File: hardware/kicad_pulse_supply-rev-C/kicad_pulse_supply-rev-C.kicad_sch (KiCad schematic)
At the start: 4 parts

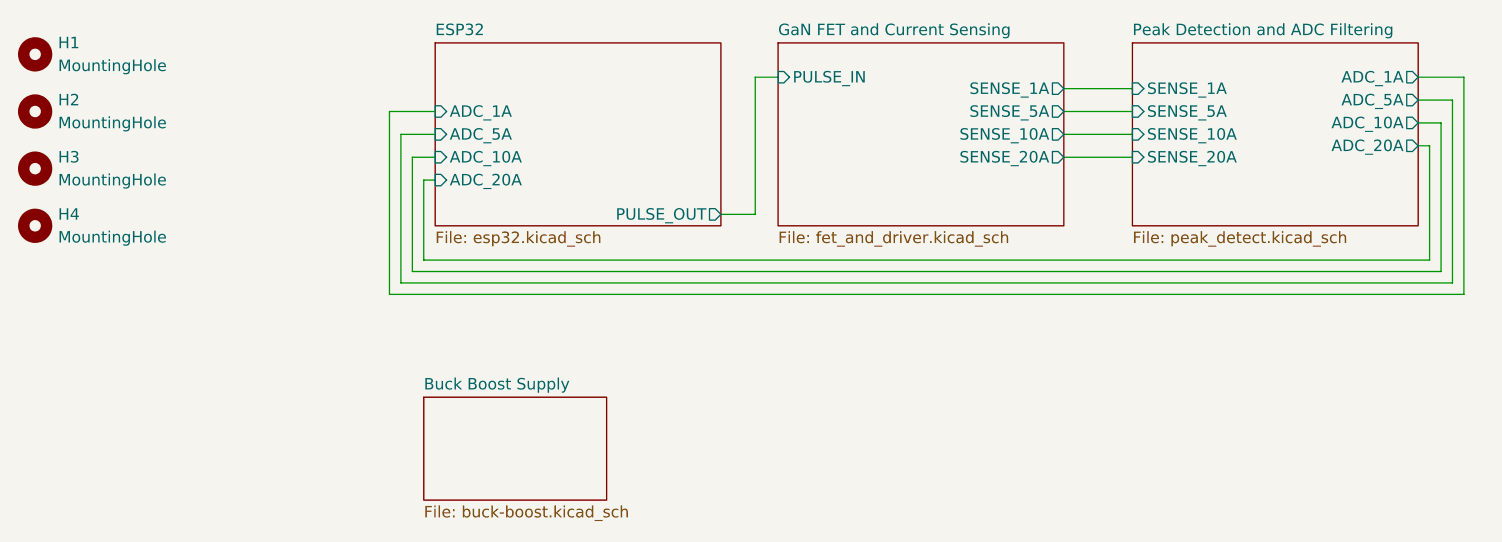
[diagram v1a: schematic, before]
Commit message: hardware breakout boards added, pcb rev-c began
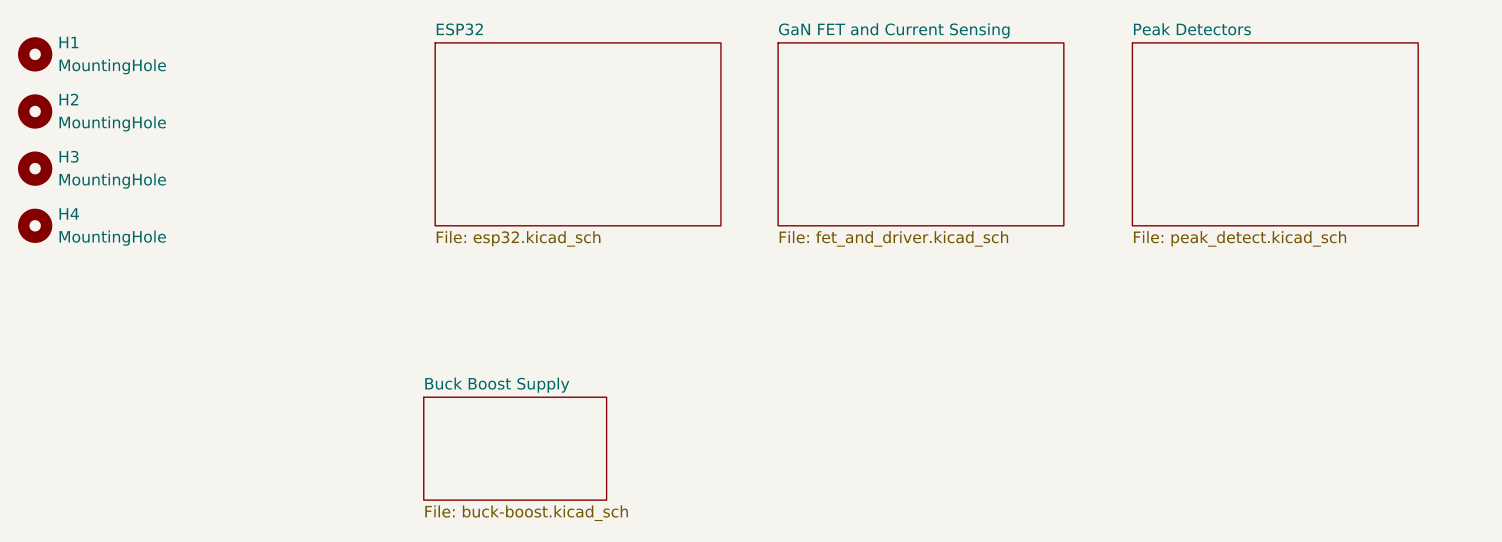
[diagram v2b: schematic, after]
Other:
- sheet Peak Detection and ADC Filtering renamed Peak Detectors
- sheet ESP32 ports: added none; removed ADC_10A, ADC_1A, ADC_20A, ADC_5A, PULSE_OUT
- sheet GaN FET and Current Sensing ports: added none; removed PULSE_IN, SENSE_10A, SENSE_1A, SENSE_20A, SENSE_5A
- sheet Peak Detectors ports: added none; removed ADC_10A, ADC_1A, ADC_20A, ADC_5A, SENSE_10A, SENSE_1A, SENSE_20A, SENSE_5A

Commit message: Rev C pcb complete, last commit before branching firmware for new board
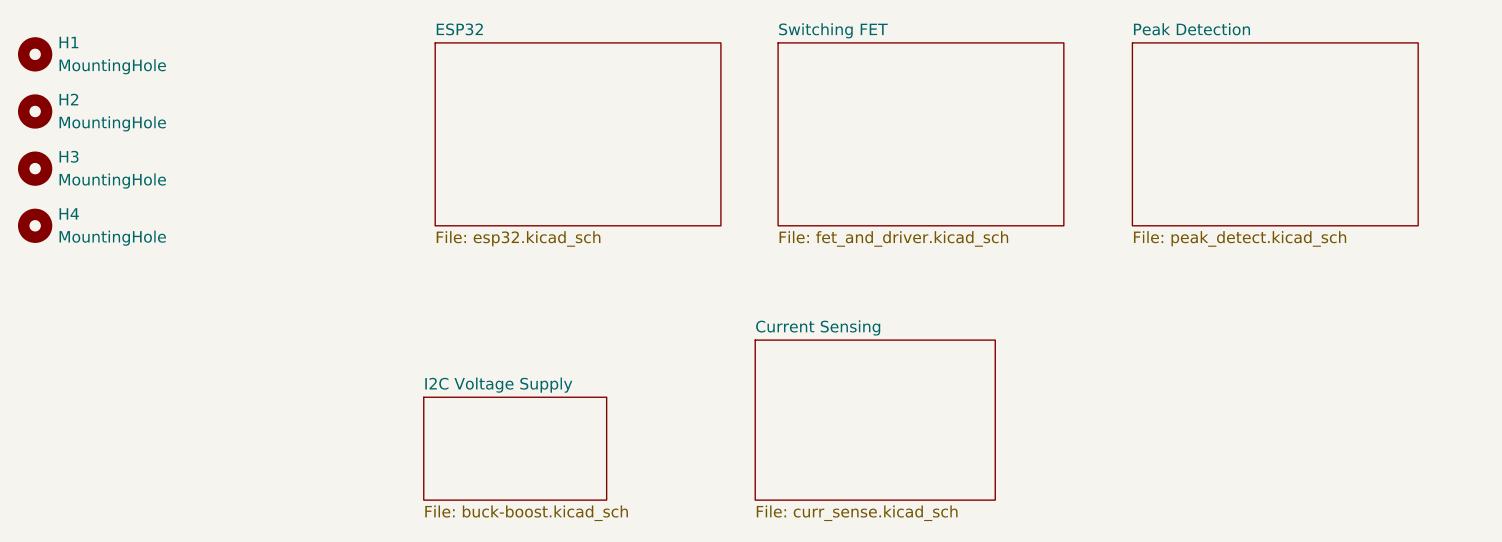
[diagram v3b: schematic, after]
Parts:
- H1, H2, H3, H4: footprint MountingHole:MountingHole_3.5mm -> MountingHole:MountingHole_3.2mm_M3
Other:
- sheet Buck Boost Supply renamed I2C Voltage Supply
- sheet GaN FET and Current Sensing renamed Switching FET
- sheet Peak Detectors renamed Peak Detection
- added sheet Current Sensing (curr_sense.kicad_sch)
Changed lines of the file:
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@@
 (kicad_sch
-	(version 20231120)
+	(version 20250114)
 	(generator "eeschema")
-	(generator_version "8.0")
+	(generator_version "9.0")
 	(paper "A4")
 	(title_block
@@
 			)
 		)
-		(property "Footprint" "MountingHole:MountingHole_3.5mm"
+		(property "Footprint" "MountingHole:MountingHole_3.2mm_M3"
 			(at 59.69 102.87 0)
 			(effects
@@
 			)
 		)
-		(property "Description" ""
+		(property "Description" "Mounting Hole without connection"
 			(at 59.69 102.87 0)
 			(effects
@@
 			)
 		)
-		(property "Footprint" "MountingHole:MountingHole_3.5mm"
+		(property "Footprint" "MountingHole:MountingHole_3.2mm_M3"
 			(at 59.69 90.17 0)
 			(effects
@@
 			)
 		)
-		(property "Description" ""
+		(property "Description" "Mounting Hole without connection"
 			(at 59.69 90.17 0)
 			(effects
@@
 			)
 		)
-		(property "Footprint" "MountingHole:MountingHole_3.5mm"
+		(property "Footprint" "MountingHole:MountingHole_3.2mm_M3"
 			(at 59.69 83.82 0)
 			(effects
@@
 			)
 		)
-		(property "Description" ""
+		(property "Description" "Mounting Hole without connection"
 			(at 59.69 83.82 0)
 			(effects
@@
 			)
 		)
-		(property "Footprint" "MountingHole:MountingHole_3.5mm"
+		(property "Footprint" "MountingHole:MountingHole_3.2mm_M3"
 			(at 59.69 96.52 0)
 			(effects
@@
 			)
 		)
-		(property "Description" ""
+		(property "Description" "Mounting Hole without connection"
 			(at 59.69 96.52 0)
 			(effects
@@
 		(at 142.24 82.55)
 		(size 31.75 20.32)
+		(exclude_from_sim no)
+		(in_bom yes)
+		(on_board yes)
+		(dnp no)
 		(fields_autoplaced yes)
 		(stroke
@@
 			(color 0 0 0 0.0000)
 		)
-		(property "Sheetname" "GaN FET and Current Sensing"
+		(property "Sheetname" "Switching FET"
 			(at 142.24 81.8384 0)
 			(effects
@@
 		(at 181.61 82.55)
 		(size 31.75 20.32)
+		(exclude_from_sim no)
+		(in_bom yes)
+		(on_board yes)
+		(dnp no)
 		(fields_autoplaced yes)
 		(stroke
@@
 			(color 0 0 0 0.0000)
 		)
-		(property "Sheetname" "Peak Detectors"
+		(property "Sheetname" "Peak Detection"
 			(at 181.61 81.8384 0)
 			(effects
@@
 			(project "kicad_pulse_supply-rev-C"
 				(path "/1c135520-adea-42af-a8f1-43758519483b"
-					(page "4")
+					(page "5")
 				)
 			)
@@
 		(at 104.14 82.55)
 		(size 31.75 20.32)
+		(exclude_from_sim no)
+		(in_bom yes)
+		(on_board yes)
+		(dnp no)
 		(fields_autoplaced yes)
 		(stroke
@@
 	)
 	(sheet
-		(at 102.87 121.92)
-		(size 20.32 11.43)
+		(at 139.7 115.57)
+		(size 26.67 17.78)
+		(exclude_from_sim no)
+		(in_bom yes)
+		(on_board yes)
+		(dnp no)
 		(fields_autoplaced yes)
 		(stroke
@@
 			(color 0 0 0 0.0000)
 		)
-		(property "Sheetname" "Buck Boost Supply"
+		(property "Sheetname" "Current Sensing"
+			(at 139.7 114.8584 0)
+			(effects
+				(font
+					(size 1.27 1.27)
+				)
+				(justify left bottom)
+			)
+		)
+		(property "Sheetfile" "curr_sense.kicad_sch"
+			(at 139.7 133.9346 0)
+			(effects
+				(font
+					(size 1.27 1.27)
+				)
+				(justify left top)
+			)
+		)
+		(instances
+			(project "kicad_pulse_supply-rev-C"
+				(path "/1c135520-adea-42af-a8f1-43758519483b"
+					(page "4")
+				)
+			)
+		)
+	)
+	(sheet
+		(at 102.87 121.92)
+		(size 20.32 11.43)
+		(exclude_from_sim no)
+		(in_bom yes)
+		(on_board yes)
+		(dnp no)
+		(fields_autoplaced yes)
+		(stroke
+			(width 0.1524)
+			(type solid)
+		)
+		(fill
+			(color 0 0 0 0.0000)
+		)
+		(property "Sheetname" "I2C Voltage Supply"
 			(at 102.87 121.2084 0)
 			(effects
@@
 			(project "kicad_pulse_supply-rev-C"
 				(path "/1c135520-adea-42af-a8f1-43758519483b"
-					(page "5")
+					(page "6")
 				)
 			)
@@
 		)
 	)
+	(embedded_fonts no)
 )
